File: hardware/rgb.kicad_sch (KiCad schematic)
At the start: 3 parts, among them U2 74AHCT1G125

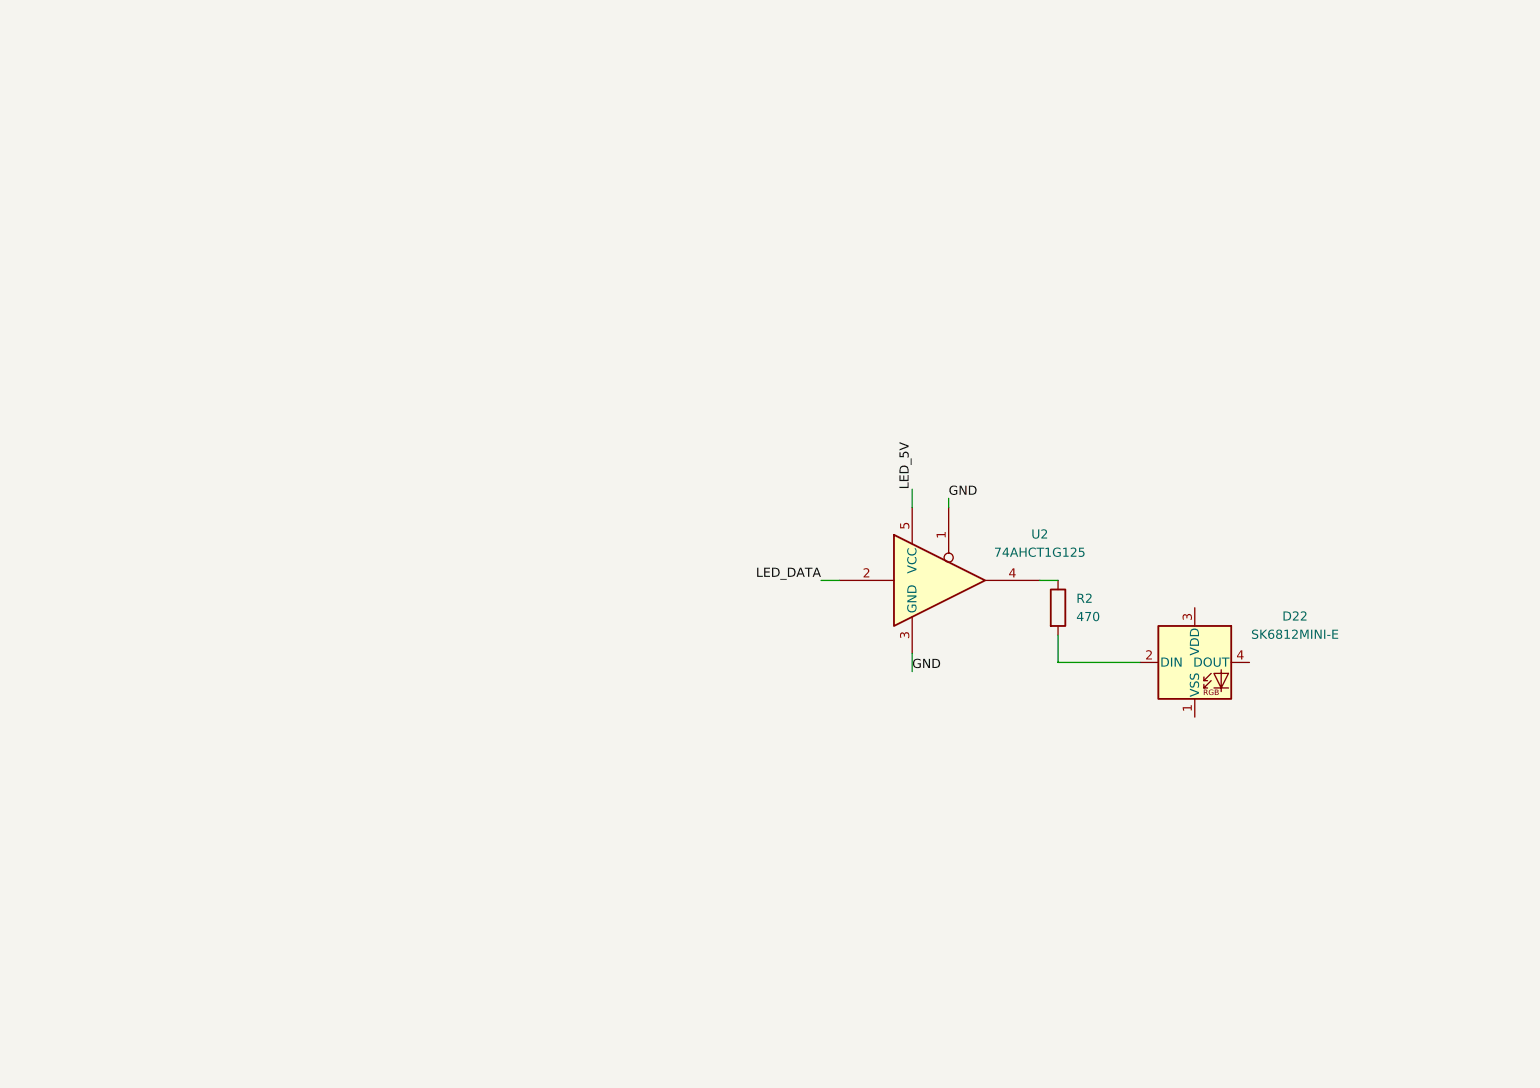
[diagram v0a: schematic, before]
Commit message: PCB: updating PCB with new RGB sch
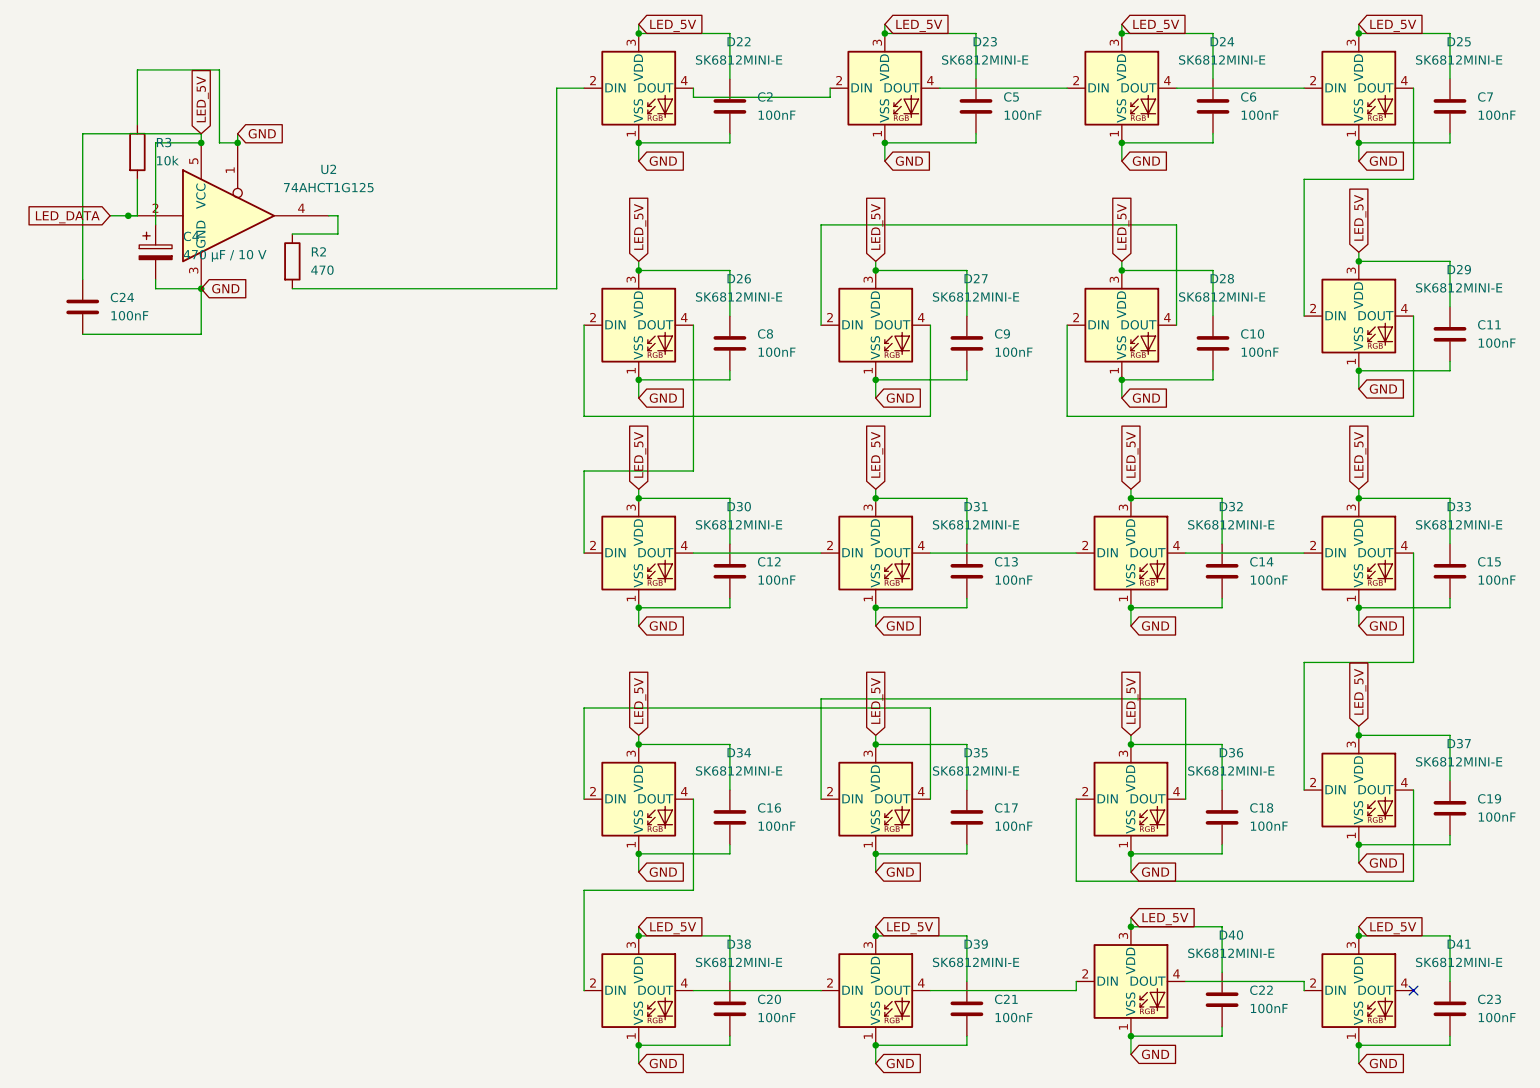
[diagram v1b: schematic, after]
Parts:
- added C10, C11, C12, C13, C14, C15, C16, C17, C18, C19, C2, C20, C21, C22, C23, C24, C5, C6, C7, C8, C9: 100nF, Capacitor_SMD:C_0805_2012Metric, symbol Device:C
- added C4: 470 µF / 10 V, Capacitor_THT:CP_Radial_D8.0mm_P3.50mm, symbol Device:C_Polarized
- added D23, D24, D25, D26, D27, D28, D29, D30, D31, D32, D33, D34, D35, D36, D37, D38, D39, D40, D41: SK6812MINI-E, LED_SMD:LED_SK6812MINI-E_3.2x2.8mm_P1.5mm_ReverseMount, symbol LED:SK6812MINI-E
- added R3: 10k, Resistor_SMD:R_0805_2012Metric, symbol Device:R
- R2: footprint (none) -> Resistor_SMD:R_0805_2012Metric
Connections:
- net GND: now also D22.1 (VSS), C10.2, C11.2, C12.2, C13.2, C14.2, C15.2, C16.2, C17.2, C18.2, C19.2, C2.2, C20.2, C21.2, C22.2, C23.2, C24.2, C4.2, C5.2, C6.2, C7.2, C8.2, C9.2, D23.1 (VSS), D24.1 (VSS), D25.1 (VSS), D26.1 (VSS), D27.1 (VSS), D28.1 (VSS), D29.1 (VSS), D30.1 (VSS), D31.1 (VSS), D32.1 (VSS), D33.1 (VSS), D34.1 (VSS), D35.1 (VSS), D36.1 (VSS), D37.1 (VSS), D38.1 (VSS), D39.1 (VSS), D40.1 (VSS), D41.1 (VSS), R3.1
- net LED_5V: now also D22.3 (VDD), C10.1, C11.1, C12.1, C13.1, C14.1, C15.1, C16.1, C17.1, C18.1, C19.1, C2.1, C20.1, C21.1, C22.1, C23.1, C24.1, C4.1, C5.1, C6.1, C7.1, C8.1, C9.1, D23.3 (VDD), D24.3 (VDD), D25.3 (VDD), D26.3 (VDD), D27.3 (VDD), D28.3 (VDD), D29.3 (VDD), D30.3 (VDD), D31.3 (VDD), D32.3 (VDD), D33.3 (VDD), D34.3 (VDD), D35.3 (VDD), D36.3 (VDD), D37.3 (VDD), D38.3 (VDD), D39.3 (VDD), D40.3 (VDD), D41.3 (VDD)
- net LED_DATA: now also R3.2
- net at D22.4 (DOUT): now also D23.2 (DIN)
- new net: D30.4 (DOUT), D31.2 (DIN)
- new net: D31.4 (DOUT), D32.2 (DIN)
- new net: D26.4 (DOUT), D30.2 (DIN)
- new net: D40.4 (DOUT), D41.2 (DIN)
- new net: D26.2 (DIN), D27.4 (DOUT)
- new net: D25.4 (DOUT), D29.2 (DIN)
- new net: D28.2 (DIN), D29.4 (DOUT)
- new net: D32.4 (DOUT), D33.2 (DIN)
- new net: D33.4 (DOUT), D37.2 (DIN)
- new net: D36.2 (DIN), D37.4 (DOUT)
- new net: D35.2 (DIN), D36.4 (DOUT)
- new net: D24.4 (DOUT), D25.2 (DIN)
- new net: D34.2 (DIN), D35.4 (DOUT)
- new net: D27.2 (DIN), D28.4 (DOUT)
- new net: D34.4 (DOUT), D38.2 (DIN)
- new net: D38.4 (DOUT), D39.2 (DIN)
- new net: D39.4 (DOUT), D40.2 (DIN)
- new net: D23.4 (DOUT), D24.2 (DIN)
- no-connect marks 0 -> 1
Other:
- title: (none) -> AKOR_01_RGB_SCH
- moved on the sheet: D22, R2, U2

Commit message: fix: link RGB schematic as hierarchical sheet
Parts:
- renumbered C9 to C10, C13 to C11, C17 to C12, C21 to C13, C5 to C14, C6 to C15, C10 to C16, C14 to C17, C22 to C19, C24 to C2, C7 to C20, C11 to C21, C15 to C22, C19 to C23, C23 to C24, C2 to C5, C8 to C6, C12 to C7, C16 to C8, C20 to C9, D26 to D23, D30 to D24, D34 to D25, D38 to D26, D31 to D28, D35 to D29, D39 to D30, D23 to D31, D24 to D32, D28 to D33, D32 to D34, D36 to D35, D40 to D36, D25 to D37, D29 to D38, D33 to D39, D37 to D40, R3 to R2, R2 to R3
